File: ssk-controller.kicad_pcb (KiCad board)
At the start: 2 copper layers, 170 x 51.5 mm, 31 parts, among them J1 Conn_01x16, J2 Conn_01x08, J3 Conn_01x01, SW1 SW_Push, U1 ATmega32U4-AU, U2 PRTR5V0U2X, Y1 16Mhz

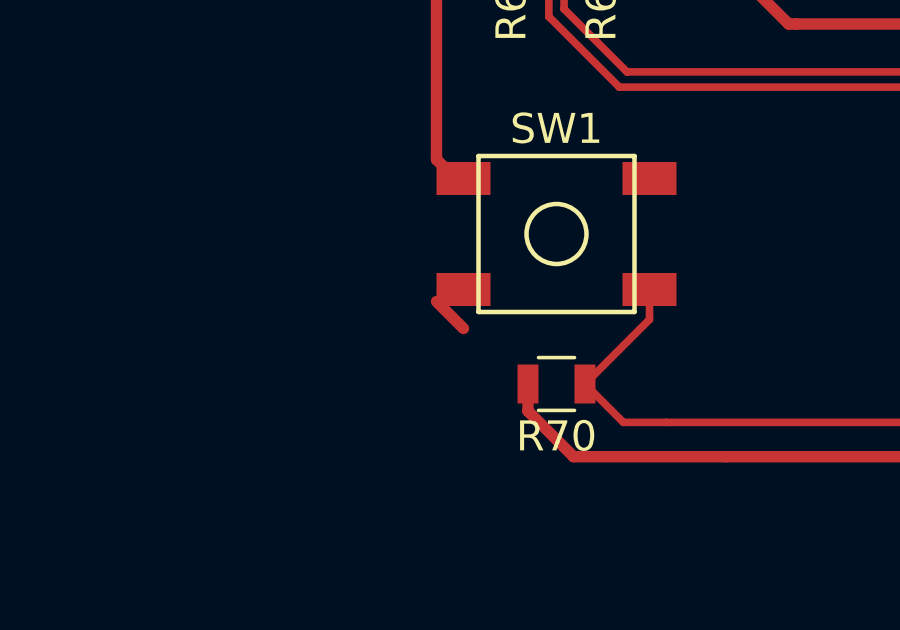
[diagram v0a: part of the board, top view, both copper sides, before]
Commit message: Update gerber, minor trace fix
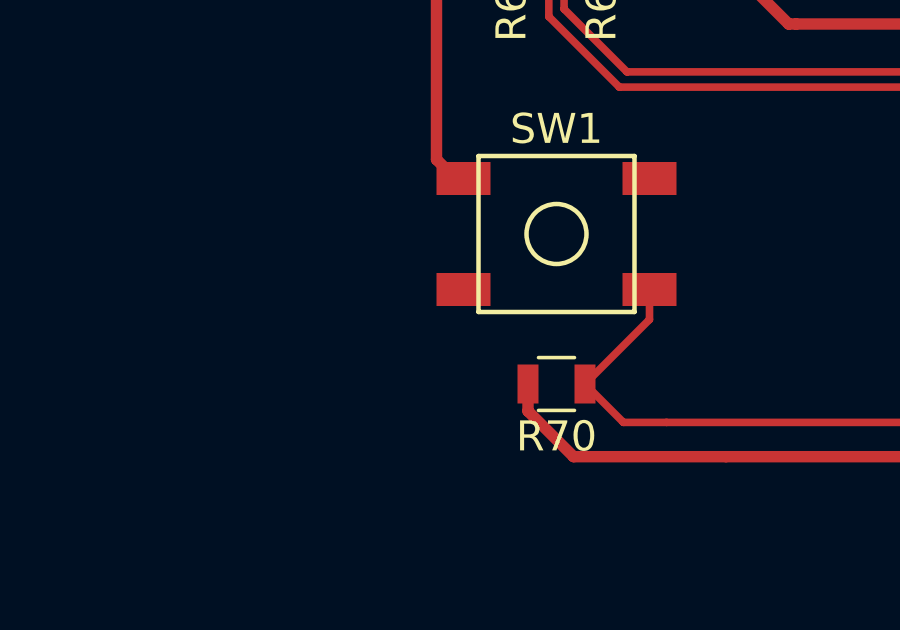
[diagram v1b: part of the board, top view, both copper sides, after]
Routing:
- net (no net): track 1.27 -> 0.00 mm
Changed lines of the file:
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@@
     (thickness 1.6)
     (drawings 60)
-    (tracks 409)
+    (tracks 408)
     (zones 0)
     (modules 31)
@@
   (segment (start 112.3 60.45) (end 114 58.75) (width 0.381) (layer F.Cu) (net 21))
   (segment (start 111 60.45) (end 112.3 60.45) (width 0.381) (layer F.Cu) (net 21))
-  (segment (start 111 77.25) (end 111.9 78.15) (width 0.381) (layer F.Cu) (net 0))
   (segment (start 120.017 60.45) (end 119 60.45) (width 0.381) (layer F.Cu) (net 21))
   (segment (start 120.017 60.454) (end 120.017 60.45) (width 0.381) (layer F.Cu) (net 21))

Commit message: Release 1.0
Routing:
- net +5V: track 111.4 -> 110.0 mm
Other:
- board text added: "Rev 1.0 20190313"
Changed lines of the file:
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@@
   (general
     (thickness 1.6)
-    (drawings 60)
-    (tracks 408)
+    (drawings 61)
+    (tracks 410)
     (zones 0)
     (modules 31)
@@
       (xy 0.003969 2.971955)) (layer B.Cu) (width 0.01))
   )
+  (gr_text "Rev 1.0 20190313" (at 105.5 94.5) (layer B.SilkS)
+    (effects (font (size 1.5 1.5) (thickness 0.3)) (justify mirror))
+  )
   (gr_text kb.ai03.me (at 223.75 94.5) (layer B.SilkS)
     (effects (font (size 1.5 1.5) (thickness 0.3)) (justify mirror))
@@
   (segment (start 149.525 76.5) (end 151 76.5) (width 0.381) (layer F.Cu) (net 7))
   (segment (start 148.725 75.7) (end 149.525 76.5) (width 0.381) (layer F.Cu) (net 7))
-  (segment (start 139.6 78.2) (end 139.6 81.634) (width 0.381) (layer F.Cu) (net 7))
-  (segment (start 138.734 82.5) (end 136 82.5) (width 0.381) (layer F.Cu) (net 7))
-  (segment (start 139.6 81.634) (end 138.734 82.5) (width 0.381) (layer F.Cu) (net 7))
   (segment (start 136.3 69.3) (end 135.3 69.3) (width 0.381) (layer F.Cu) (net 7))
   (segment (start 134 68) (end 133 68) (width 0.381) (layer F.Cu) (net 7))
@@
   (segment (start 114.05 80.903) (end 114.05 80) (width 0.381) (layer F.Cu) (net 7))
   (segment (start 115.57 82.423) (end 114.05 80.903) (width 0.381) (layer F.Cu) (net 7))
+  (segment (start 136 82.5) (end 136.448 82.5) (width 0.381) (layer F.Cu) (net 7))
+  (segment (start 139.6 79.348) (end 139.6 78.994) (width 0.381) (layer F.Cu) (net 7))
+  (segment (start 136.448 82.5) (end 139.6 79.348) (width 0.381) (layer F.Cu) (net 7))
+  (segment (start 139.6 78.2) (end 139.6 78.994) (width 0.381) (layer F.Cu) (net 7))
   (segment (start 136.3 75.7) (end 135.374 75.7) (width 0.254) (layer F.Cu) (net 8))
   (segment (start 135.374 75.7) (end 134.747 76.327) (width 0.254) (layer F.Cu) (net 8))
@@
   (segment (start 117.094 70.104) (end 134.493 70.104) (width 0.254) (layer F.Cu) (net 29))
   (segment (start 134.493 70.104) (end 135.289 70.9) (width 0.254) (layer F.Cu) (net 29))
+  (segment (start 115.95 79.747) (end 118.1 77.597) (width 0.254) (layer F.Cu) (net 30))
+  (segment (start 115.95 80) (end 115.95 79.747) (width 0.254) (layer F.Cu) (net 30))
+  (segment (start 118.1 76.85) (end 118.1 77.597) (width 0.254) (layer F.Cu) (net 30))
+  (segment (start 115.95 80.263) (end 115.95 80) (width 0.254) (layer F.Cu) (net 30))
+  (segment (start 116.967 81.28) (end 115.95 80.263) (width 0.254) (layer F.Cu) (net 30))
+  (segment (start 136.779 81.28) (end 116.967 81.28) (width 0.254) (layer F.Cu) (net 30))
   (segment (start 138.8 78.2) (end 138.8 79.259) (width 0.254) (layer F.Cu) (net 30))
   (segment (start 138.8 79.259) (end 136.779 81.28) (width 0.254) (layer F.Cu) (net 30))
-  (segment (start 136.779 81.28) (end 118.67 81.28) (width 0.254) (layer F.Cu) (net 30))
-  (segment (start 118.1 77.85) (end 115.95 80) (width 0.254) (layer F.Cu) (net 30))
-  (segment (start 118.1 76.85) (end 118.1 77.85) (width 0.254) (layer F.Cu) (net 30))
-  (segment (start 117.23 81.28) (end 115.95 80) (width 0.254) (layer F.Cu) (net 30))
-  (segment (start 118.67 81.28) (end 117.23 81.28) (width 0.254) (layer F.Cu) (net 30))
   (segment (start 148.717 68.5) (end 147.7 68.5) (width 0.254) (layer F.Cu) (net 31))
   (segment (start 149.267 67.95) (end 148.717 68.5) (width 0.254) (layer F.Cu) (net 31))
@@
     (polygon
       (pts
-        (xy 150.5 80.5) (xy 150.5 93.5) (xy 137 93.5) (xy 137 80.5)
+        (xy 150.5 79.5) (xy 150.5 93.5) (xy 137 93.5) (xy 137 79.5)
       )
     )

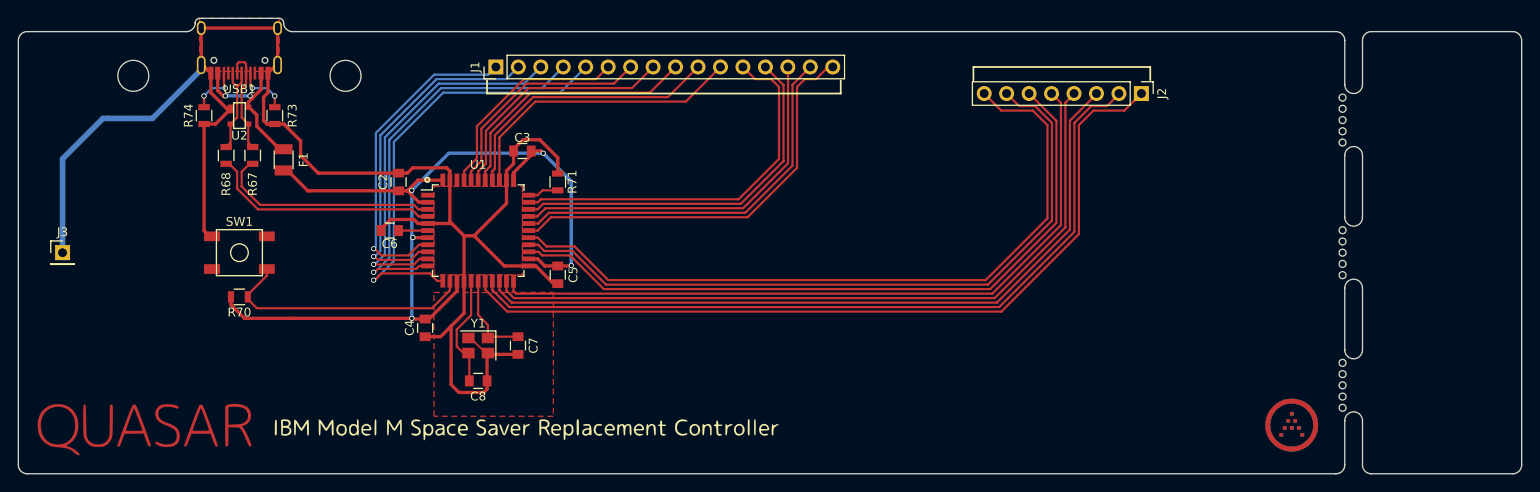
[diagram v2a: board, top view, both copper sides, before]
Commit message: New gerbers for USB B
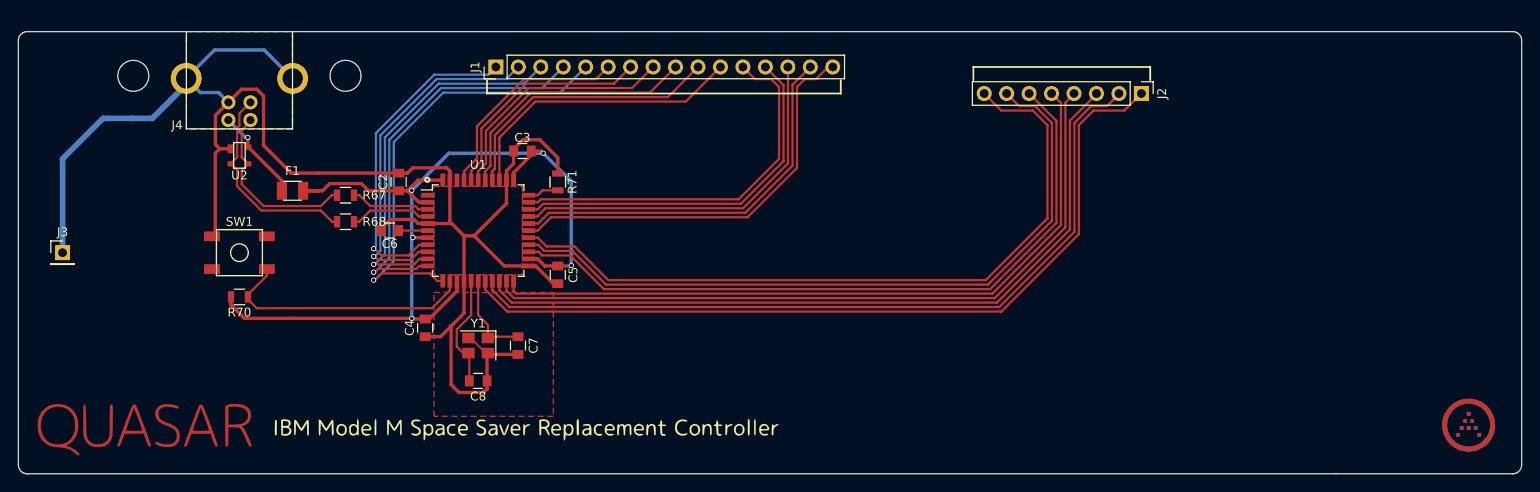
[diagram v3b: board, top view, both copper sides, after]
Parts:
- removed the G*** at (234.0, 94.5) (x2)
- removed R73, R74: 5.1k, Resistors_SMD:R_0805
- removed the REF** at (240.0, 75.0)
- removed the REF** at (240.0, 60.0)
- removed the REF** at (240.0, 90.0)
- removed USB1: HRO-TYPE-C-31-M-12, Type-C:HRO-TYPE-C-31-M-12-Assembly
- added G***: LOGO, locallib:ai-ring-6mm-Combined, F.Cu at (254.0, 94.5)
- added G***: LOGO, locallib:ai-ring-6mm-Combined, B.Cu at (254.0, 94.5)
- added J4: USB_B, locallib:TE-292304-2, F.Cu at (115.0, 60.0)
- moved R68 15.4 mm to (127.0, 71.5), turned to 180 degrees
- moved R67 11.4 mm to (127.0, 68.5), turned to 180 degrees
- moved U2 4.50 mm to (115.0, 64.0)
- moved F1 3.64 mm to (121.0, 68.0), turned to 180 degrees
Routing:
- net D+: track 26.4 -> 9.15 mm
- net D-: track 25.4 -> 9.01 mm
- net Net-(J4-Pad3): track 10.8 -> 23.8 mm
- net Net-(J4-Pad2): track 12.3 -> 20.6 mm
- net VCC: track 17.4 -> 10.7 mm, vias 2 -> 1
- net Net-(R73-Pad2): track 5.96 -> 0.00 mm, vias 2 -> 0
- net Net-(R74-Pad2): track 5.81 -> 0.00 mm, vias 2 -> 0
- net GND: track 188.8 -> 185.5 mm
- net +5V: track 110.0 -> 108.8 mm
- added copper zone on B.Cu, net GND
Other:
- board size 170 x 51.5 mm -> 170 x 50 mm
- board text added: "Rev 1.1 20190527"
- board text removed: "150mm"
- board text removed: "170mm"
- board text removed: "Break off tab if original controller size is 150mm"
- board text removed: "Rev 1.0 20190313"

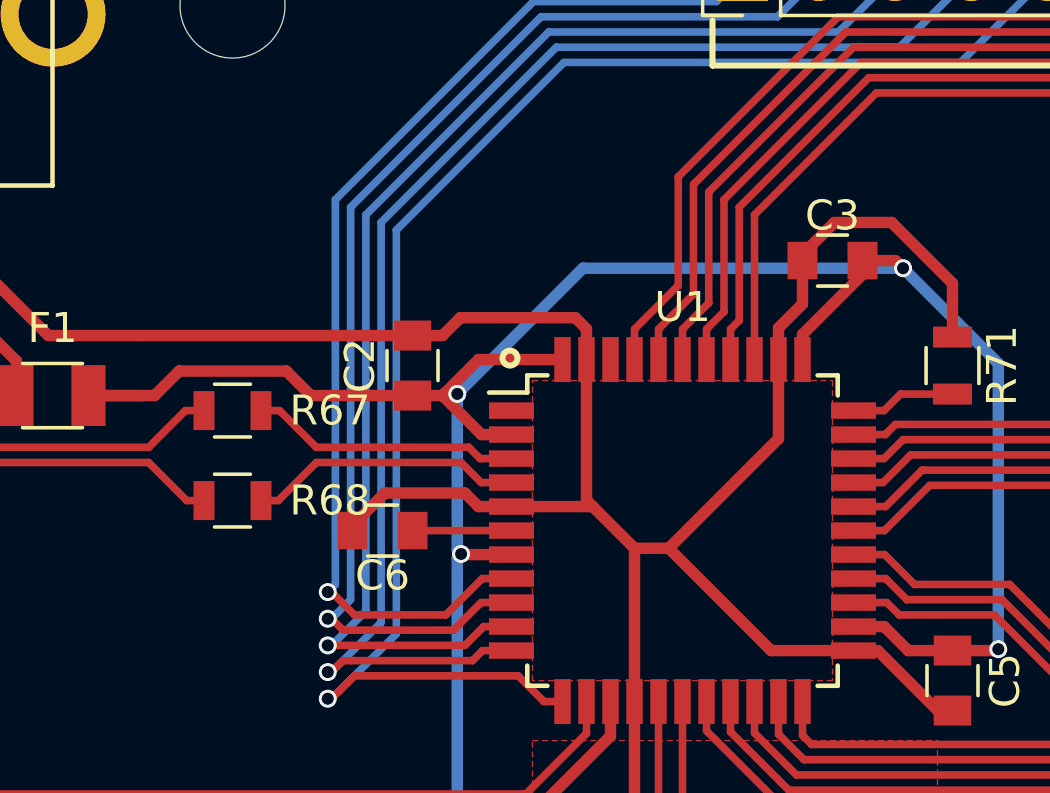
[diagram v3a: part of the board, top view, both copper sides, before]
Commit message: Tune silkscreen
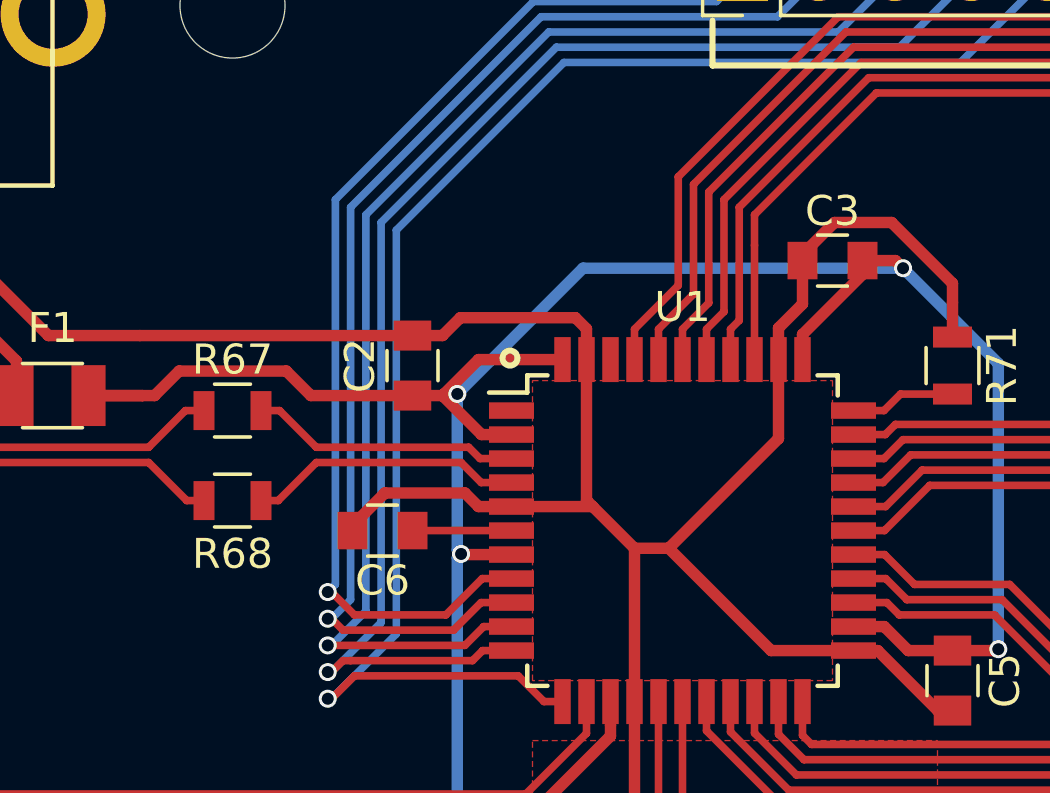
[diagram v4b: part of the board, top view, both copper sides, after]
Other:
- board text added: "Rev 1.2 20190527"
- board text removed: "Rev 1.1 20190527"
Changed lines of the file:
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@@
     (tags "resistor 0805")
     (attr smd)
-    (fp_text reference R67 (at -3.25 0) (layer F.SilkS)
+    (fp_text reference R67 (at 0 1.698) (layer F.SilkS)
       (effects (font (size 1 1) (thickness 0.15)))
     )
@@
     (tags "resistor 0805")
     (attr smd)
-    (fp_text reference R68 (at -3.25 0) (layer F.SilkS)
+    (fp_text reference R68 (at 0 -1.779) (layer F.SilkS)
       (effects (font (size 1 1) (thickness 0.15)))
     )
@@
     (tags "capacitor 0805")
     (attr smd)
-    (fp_text reference C3 (at 0 -1.5) (layer F.SilkS)
+    (fp_text reference C3 (at 0 -1.651) (layer F.SilkS)
       (effects (font (size 1 1) (thickness 0.15)))
     )
@@
     (tags "capacitor 0805")
     (attr smd)
-    (fp_text reference C6 (at 0 -1.5 180) (layer F.SilkS)
+    (fp_text reference C6 (at 0 -1.668 180) (layer F.SilkS)
       (effects (font (size 1 1) (thickness 0.15)))
     )
@@
   (gr_line (start 121 61) (end 109 61) (layer F.SilkS) (width 0.15))
   (gr_line (start 121 50) (end 121 61) (layer F.SilkS) (width 0.15))
-  (gr_text "Rev 1.1 20190527" (at 105.5 94.5) (layer B.SilkS)
+  (gr_text "Rev 1.2 20190527" (at 105.5 94.5) (layer B.SilkS)
     (effects (font (size 1.5 1.5) (thickness 0.3)) (justify mirror))
   )

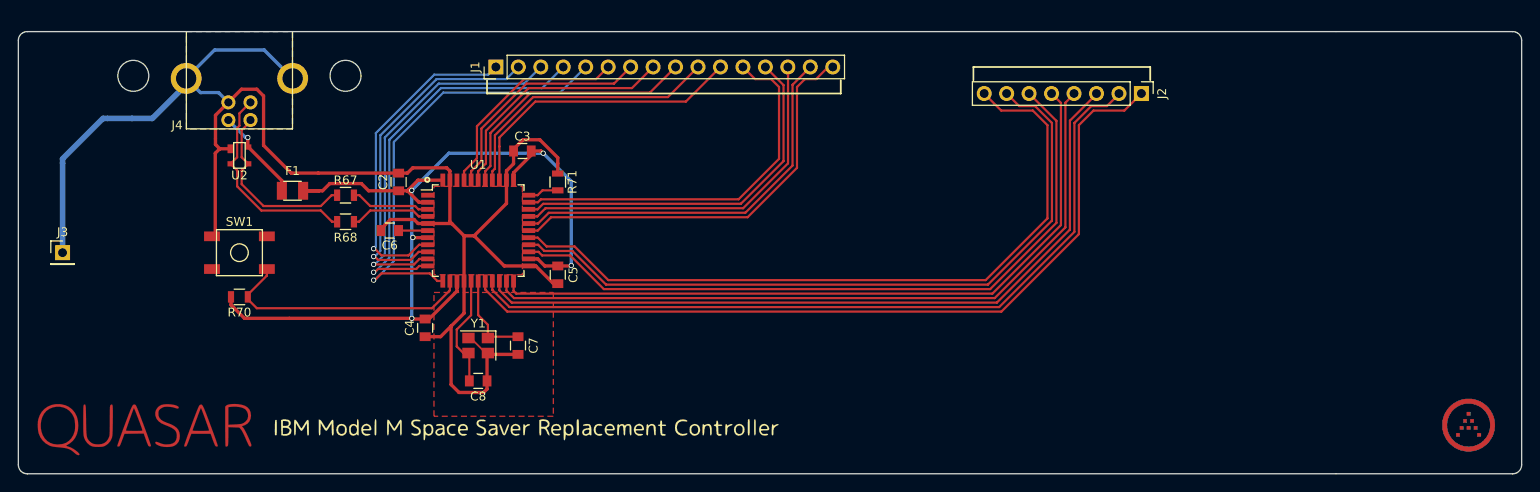
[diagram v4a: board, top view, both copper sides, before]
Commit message: Add solenoid support and better ESD handling
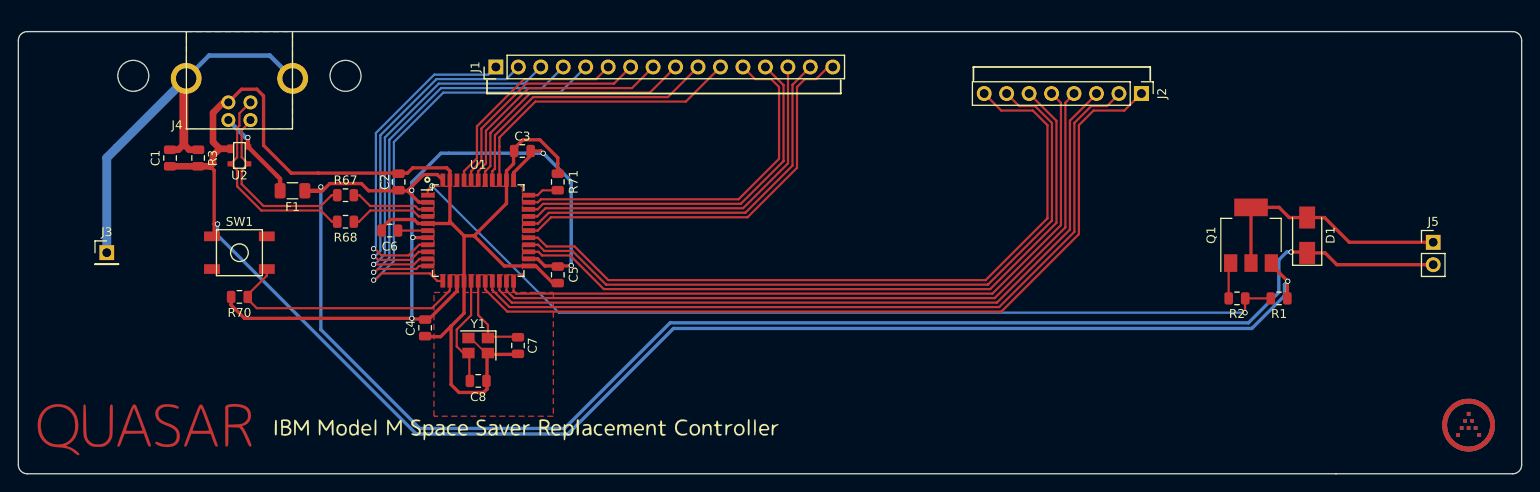
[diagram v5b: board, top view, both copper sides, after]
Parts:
- added C1: 4.7nF, Capacitor_SMD:C_0805_2012Metric, F.Cu at (107.2, 64.3)
- added D1: 1N4007, Diode_SMD:D_SMA, F.Cu at (235.7, 73.0)
- added J5: Solenoid, Connector_PinHeader_2.54mm:PinHeader_1x02_P2.54mm_Vertical, F.Cu at (250.0, 73.8)
- added Q1: Q_NMOS_GDS, Package_TO_SOT_SMD:SOT-223-3_TabPin2, F.Cu at (229.4, 73.0)
- added R1: 1M, Resistor_SMD:R_0805_2012Metric, F.Cu at (232.6, 80.2)
- added R2: 100, Resistor_SMD:R_0805_2012Metric, F.Cu at (227.8, 80.2)
- added R3: 1M, Resistor_SMD:R_0805_2012Metric, F.Cu at (110.3, 64.3)
- C2, C3, C4, C5, C6, C7, C8: footprint Capacitors_SMD:C_0805 -> Capacitor_SMD:C_0805_2012Metric
- F1: footprint Fuse_Holders_and_Fuses:Fuse_SMD1206_Reflow -> Fuse:Fuse_1206_3216Metric
- J1: footprint Pin_Headers:Pin_Header_Straight_1x16_Pitch2.54mm -> Connector_PinHeader_2.54mm:PinHeader_1x16_P2.54mm_Vertical
- J2: footprint Pin_Headers:Pin_Header_Straight_1x08_Pitch2.54mm -> Connector_PinHeader_2.54mm:PinHeader_1x08_P2.54mm_Vertical
- J3: footprint Pin_Headers:Pin_Header_Straight_1x01_Pitch2.54mm -> Connector_PinHeader_2.54mm:PinHeader_1x01_P2.54mm_Vertical
- R67, R68, R70, R71: footprint Resistors_SMD:R_0805 -> Resistor_SMD:R_0805_2012Metric
- U1: footprint Housings_QFP:TQFP-44_10x10mm_Pitch0.8mm -> Package_QFP:TQFP-44_10x10mm_P0.8mm
- Y1: footprint Crystals:Crystal_SMD_3225-4pin_3.2x2.5mm -> Crystal:Crystal_SMD_3225-4Pin_3.2x2.5mm
- moved J3 5.00 mm to (100.0, 75.0)
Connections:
- J3 pad 1: GND -> Earth
- J4 pad 5: GND -> Earth
- U1 pad 1: Net-(U1-Pad1) -> SOLENOID
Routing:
- net +5V: track 108.8 -> 267.8 mm, vias 5 -> 7
- net SOLENOID: track 0.00 -> 103.7 mm, vias 0 -> 2
- net GND: track 185.5 -> 286.2 mm, vias 0 -> 2
- net Earth: track 0.00 -> 48.9 mm
- net Net-(D1-Pad2): track 0.00 -> 28.5 mm
- net Net-(Q1-Pad1): track 0.00 -> 4.09 mm
- added copper zone on B.Cu, net Earth
- removed copper zone on B.Cu, net GND
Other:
- net class Earth added: clearance 0.2032, trace_width 0.5, via_dia 0.6, via_drill 0.4
- board text added: "5V solenoid"
- board text added: "Connection to backplate"
- board text removed: "Ground pad for connection to backplate"

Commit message: Cleanup traces
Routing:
- net +5V: track 267.8 -> 266.4 mm
- net GND: track 286.2 -> 285.3 mm
